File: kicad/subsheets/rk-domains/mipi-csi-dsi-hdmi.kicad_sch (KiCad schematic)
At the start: 11 parts, among them U5 RK3566

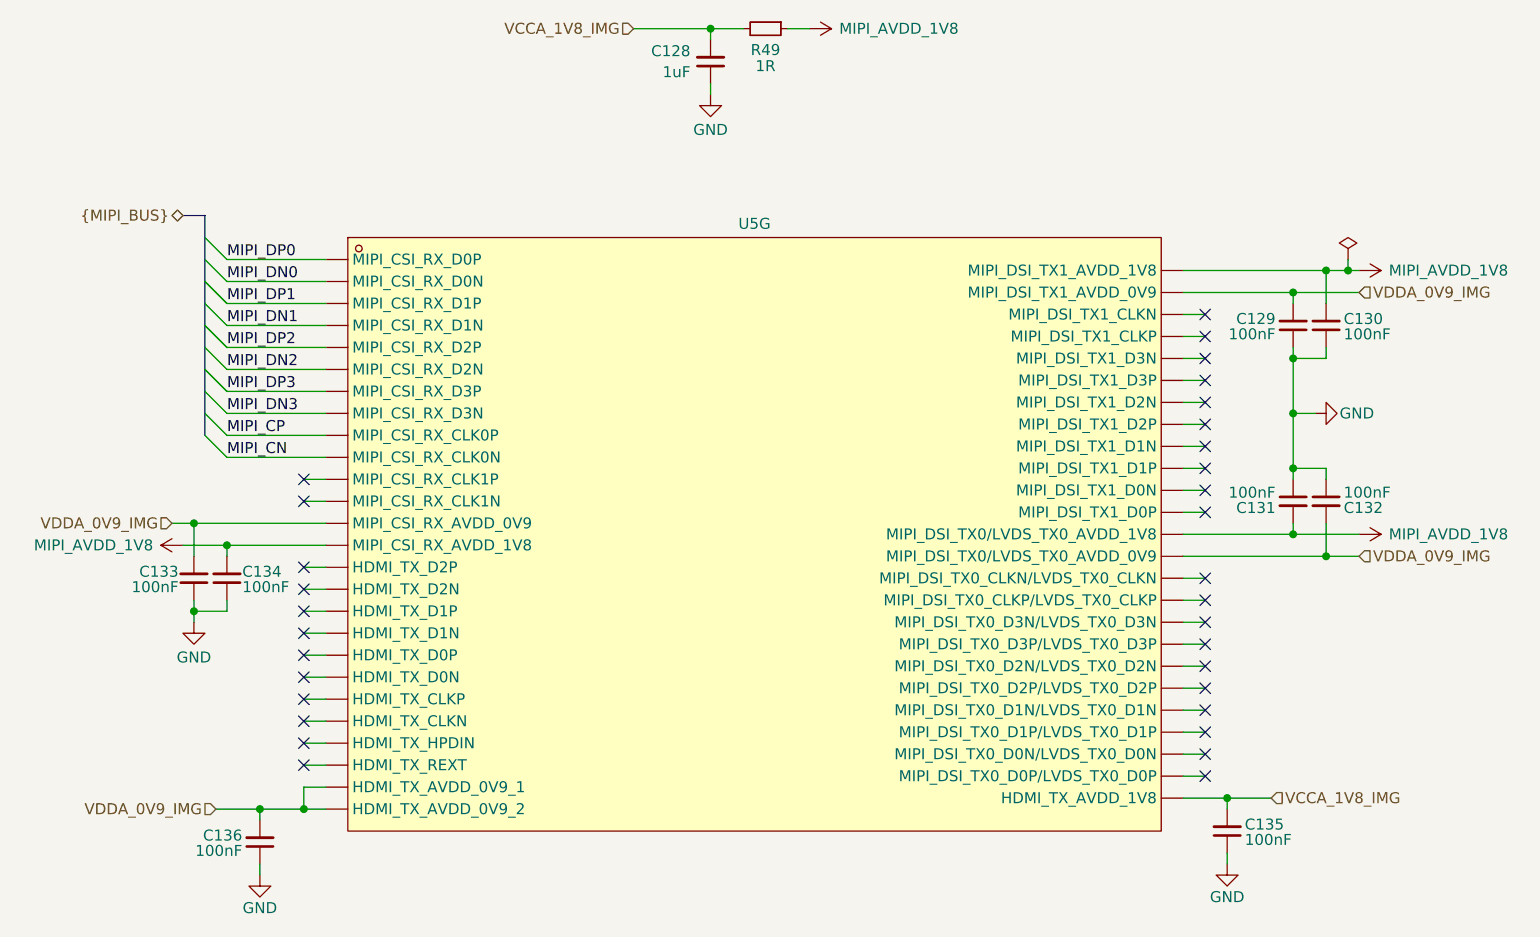
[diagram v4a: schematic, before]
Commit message: Remove power/decoupling for unused power domains
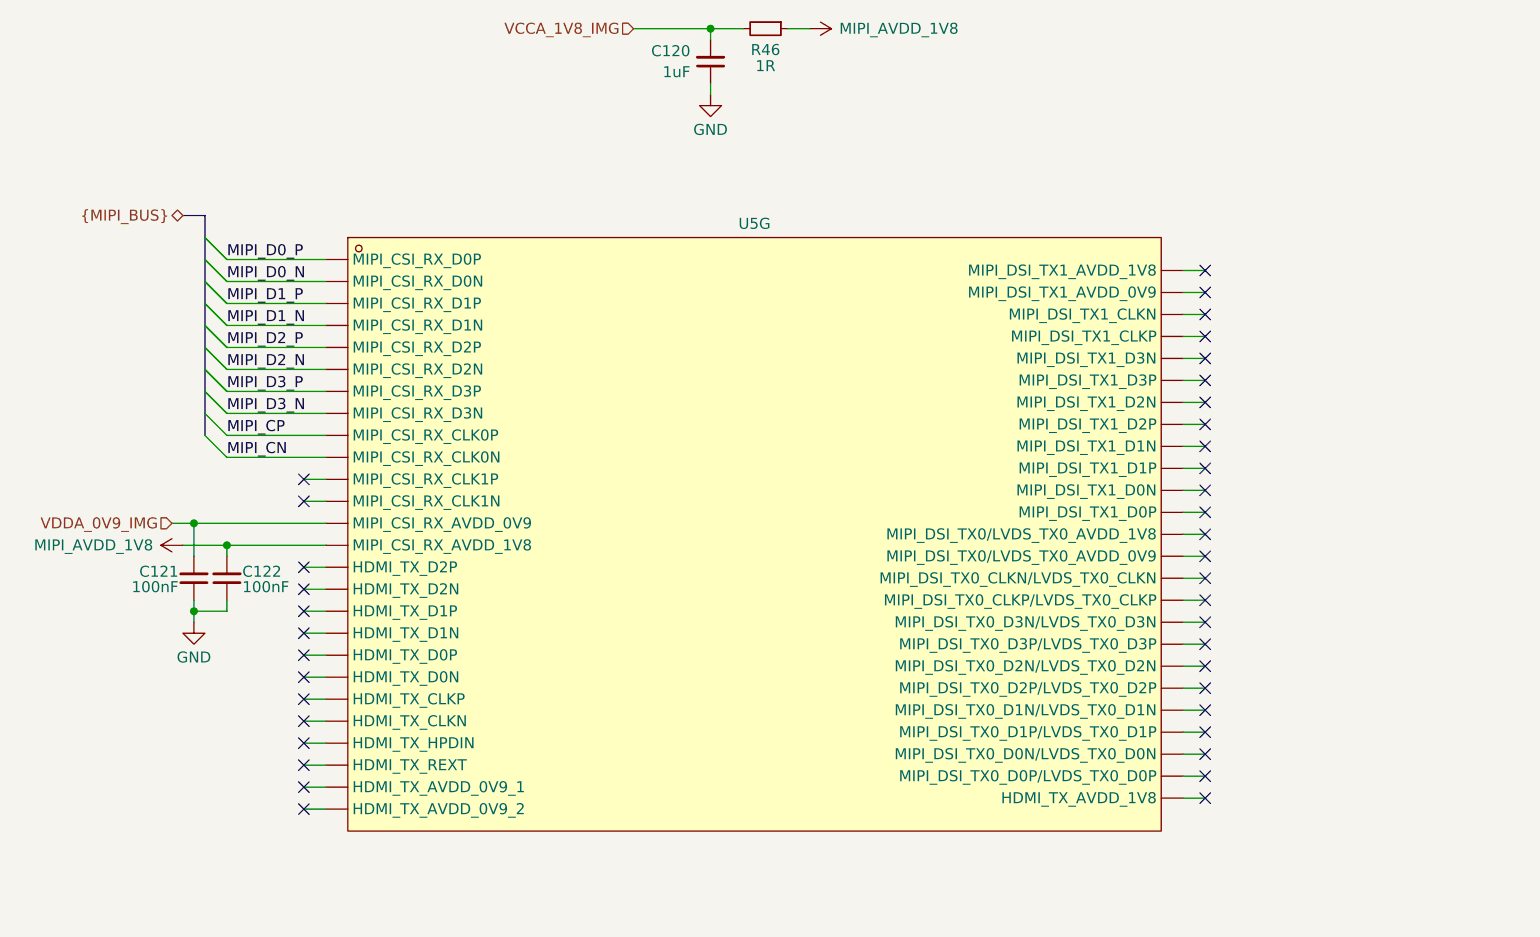
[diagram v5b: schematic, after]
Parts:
- removed C129, C130, C131, C132, C135, C136: 100nF, Capacitor_SMD:C_0402_1005Metric, symbol Device:C_Small
- renumbered C128 to C120, C133 to C121, C134 to C122, R49 to R46
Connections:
- net MIPI_AVDD_1V8: no longer U5.1P12 (MIPI_DSI_TX0/LVDS_TX0_AVDD_1V8), U5.1R10 (MIPI_DSI_TX1_AVDD_1V8)
- net VCCA_1V8_IMG: no longer U5.1P13 (HDMI_TX_AVDD_1V8)
- net VDDA_0V9_IMG: no longer U5.1N10 (MIPI_DSI_TX1_AVDD_0V9), U5.1N13 (HDMI_TX_AVDD_0V9_2), U5.1N14 (HDMI_TX_AVDD_0V9_1), U5.1P11 (MIPI_DSI_TX0/LVDS_TX0_AVDD_0V9)
- net MIPI_DN0 renamed MIPI_D0_N
- net MIPI_DN1 renamed MIPI_D1_N
- net MIPI_DN2 renamed MIPI_D2_N
- net MIPI_DN3 renamed MIPI_D3_N
- net MIPI_DP0 renamed MIPI_D0_P
- net MIPI_DP1 renamed MIPI_D1_P
- net MIPI_DP2 renamed MIPI_D2_P
- net MIPI_DP3 renamed MIPI_D3_P
- no-connect marks 32 -> 39
